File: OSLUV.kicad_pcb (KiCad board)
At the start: 4 copper layers, 110 x 40 mm, 160 parts, among them IC1 OPA2356AIDGKR, IC2 LM2901, IC3 STM32G071KBT6, IC4 INA210, IC5 AP63300WU-7, IC6 AP63300WU-7, IC7 LP2985-33DBVR, IC8 1ED44175N01BXTSA1, J1 B04B-XASK-1_LF__SN_, J2 B08B-XASK-1-A_LF__SN_, J3 TC2030, J4 BM02B-SRSS-TB_LF__SN_, J5 B4B-PH-K-S_LF__SN_, J6 B5P-VH, M1 K 274 MI 247 V, M2 KU-CG20, T101 IMZC120R078M2H, T2 DCX114EU-7-F, T3 BC817-40, T4 DCX114EU-7-F, T5 DCX114EU-7-F

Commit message: Fixed BoM, and added jobset.
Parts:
- C30, C31, C36, C37, C39: value 10u X7R 1210 -> 10µ X7R 1210
- J6: value B5P-VH -> B2P5-VH
- M2: value KU-CG20 -> Silicone gap pad, 200µm, Ubd≥5kV, λ≥1.9 W/mK. 24 x 22 mm. Acc. to drawing from 08.01.2026
- R67, R68: value 1Meg 0.1% 500V 1206 -> 1M 1% 500V 1206

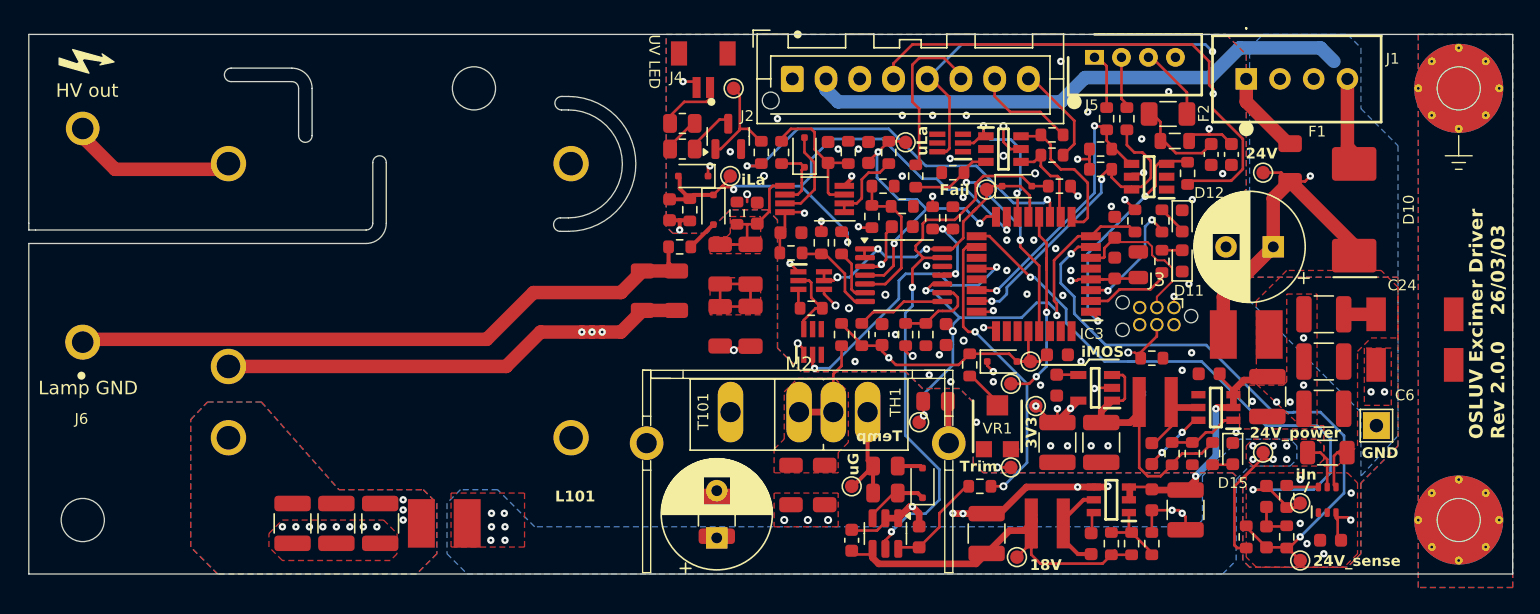
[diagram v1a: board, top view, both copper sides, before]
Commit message: Fixed debug header footprint, and cleaned up silkscreen.
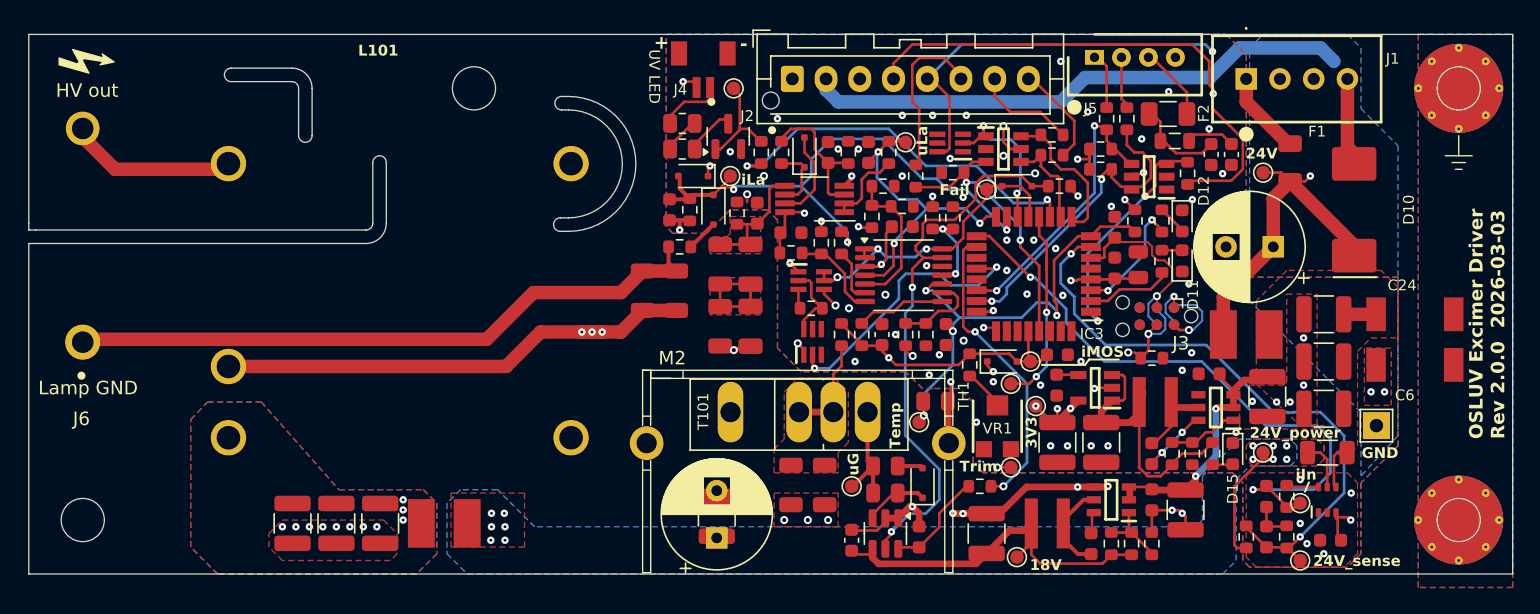
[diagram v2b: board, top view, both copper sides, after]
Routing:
- net /excimerDriver/SWDIO: track 16.6 -> 22.9 mm, vias 1 -> 2
- net /excimerDriver/SWCLK: track 16.6 -> 19.9 mm, vias 2 -> 3
- net +3V3: track 44.6 -> 47.5 mm
- net /excimerDriver/RESET: track 12.1 -> 14.7 mm, vias 0 -> 1
- net GND: track 122.8 -> 124.3 mm, vias 88 -> 87
- net /excimerDriver/Isense_In: track 46.8 -> 46.3 mm
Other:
- board text added: "+"
- board text added: "-"
- board text added: "OSLUV Excimer Driver Rev 2.0.0 2026-03-03"
- board text removed: "OSLUV Excimer Driver Rev 2.0.0 26/03/03"

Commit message: Fixed transformer footprint, and cleaned up silkscreen.
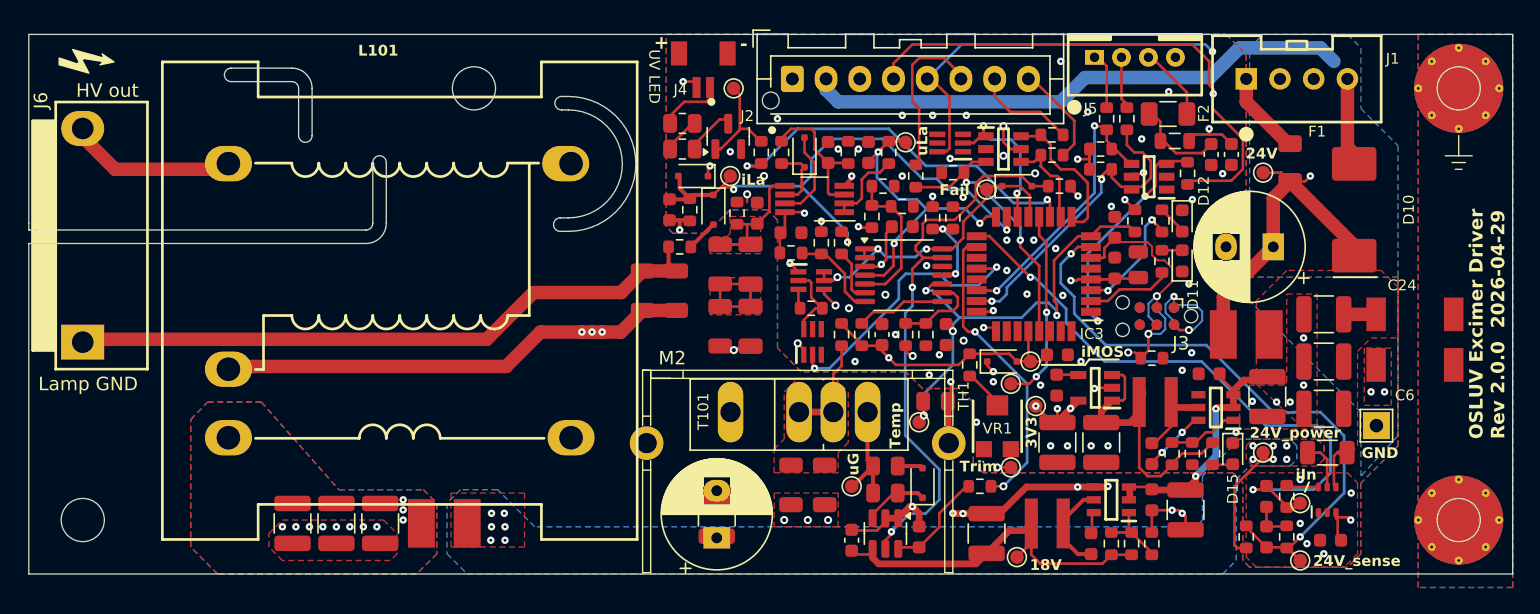
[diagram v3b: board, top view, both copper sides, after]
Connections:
- L101 pad 5: /excimerDriver/lampDriver/VDC_Trafo -> GND
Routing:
- net Net-(IC3-PA5): track 15.4 -> 14.5 mm
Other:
- board text added: "13"
- board text added: "2"
- board text added: "5"
- board text added: "6"
- board text added: "9"
- board text added: "OSLUV Excimer Driver Rev 2.0.0 2026-04-29"
- board text removed: "OSLUV Excimer Driver Rev 2.0.0 2026-03-03"
